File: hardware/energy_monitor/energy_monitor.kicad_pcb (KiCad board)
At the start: 2 copper layers, 102.8 x 86.9 mm, 137 parts, among them J1 Screw_Terminal_01x03, J2 SJ1-3533NG, J3 SJ1-3533NG, J4 SJ1-3533NG, J5 SJ1-3533NG, J6 SJ1-3533NG, J7 SJ1-3533NG, J8 USB_OTG, Q1 MMBT2222, Q2 MMBT2222, U1 RAC04, U2 TPS730, U3 TPS723, U4 ADS131E08, U5 AP2112, U6 ESP-WROOM-32U, U7 CP2104

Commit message: Working on layout
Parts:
- F1, F2: footprint Fuse_Holders_and_Fuses:Fuseholder5x20_horiz_open_inline_Type-I -> footprint:Fuse_Littelfuse-443
- RV1, RV2: footprint Varistors:RV_Disc_D15.5_W6.8_P7.5 -> Varistors:RV_Disc_D12_W5_P7.5
- moved U7 114.8 mm to (159.0, 53.1)
- moved RV1 93.6 mm to (100.7, 90.7), turned to 270 degrees
- moved F2 84.8 mm to (111.0, 94.5), turned to 270 degrees
- moved F1 79.5 mm to (93.8, 94.5), turned to 270 degrees
- moved C15 65.2 mm to (31.3, 110.9)
- moved U3 63.7 mm to (48.0, 121.7)
- moved U5 55.2 mm to (60.2, 114.9)
- moved RV2 54.3 mm to (104.3, 98.2), turned to 90 degrees
- moved U2 48.3 mm to (35.3, 127.4)
- moved C16 47.9 mm to (45.1, 108.9)
- moved U6 26.4 mm to (178.3, 57.0)
- moved J8 22.7 mm to (158.7, 33.0)
- moved J2 13.8 mm to (120.0, 119.0)
- moved U4 13.5 mm to (146.4, 76.3)
- moved J4 13.1 mm to (152.8, 119.0)
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
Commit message: Configured design rules
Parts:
- moved Q1 35.5 mm to (30.1, 139.3)
- moved Q2 35.5 mm to (40.4, 136.9)
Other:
- copper layers 2 -> 4
- net class Default: clearance 0.2 -> 0.1524; trace_width 0.25 -> 0.1524; via_dia 0.6 -> 0.452; via_drill 0.4 -> 0.3
- rule trace_clearance: 0.2 -> 0.1524
- rule trace_min: 0.2 -> 0.1524
- rule via_min_size: 0.4 -> 0.452
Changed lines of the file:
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@@
     (links 312)
     (no_connects 312)
-    (area 89.924999 33.024999 192.875001 120.075001)
+    (area 26.374999 31.525 192.900001 188.72)
     (thickness 1.6)
     (drawings 14)
@@
   (layers
     (0 F.Cu signal)
+    (1 In1.Cu signal)
+    (2 In2.Cu signal)
     (31 B.Cu signal)
-    (32 B.Adhes user)
-    (33 F.Adhes user)
-    (34 B.Paste user)
-    (35 F.Paste user)
+    (34 B.Paste user hide)
+    (35 F.Paste user hide)
     (36 B.SilkS user)
     (37 F.SilkS user)
-    (38 B.Mask user)
-    (39 F.Mask user)
-    (40 Dwgs.User user)
-    (41 Cmts.User user)
+    (38 B.Mask user hide)
+    (39 F.Mask user hide)
+    (40 Dwgs.User user hide)
     (42 Eco1.User user)
-    (43 Eco2.User user)
     (44 Edge.Cuts user)
-    (45 Margin user)
-    (46 B.CrtYd user)
-    (47 F.CrtYd user)
-    (48 B.Fab user)
+    (48 B.Fab user hide)
     (49 F.Fab user)
   )
   (setup
-    (last_trace_width 0.25)
-    (trace_clearance 0.2)
+    (last_trace_width 0.1524)
+    (user_trace_width 0.16)
+    (user_trace_width 0.2)
+    (user_trace_width 0.3)
+    (user_trace_width 0.4)
+    (trace_clearance 0.1524)
     (zone_clearance 0.508)
     (zone_45_only no)
-    (trace_min 0.2)
+    (trace_min 0.1524)
     (segment_width 0.2)
     (edge_width 0.15)
-    (via_size 0.6)
-    (via_drill 0.4)
-    (via_min_size 0.4)
+    (via_size 0.452)
+    (via_drill 0.3)
+    (via_min_size 0.452)
     (via_min_drill 0.3)
-    (uvia_size 0.3)
-    (uvia_drill 0.1)
+    (user_via 0.452 0.3)
+    (user_via 0.552 0.4)
+    (uvia_size 0.452)
+    (uvia_drill 0.3)
     (uvias_allowed no)
-    (uvia_min_size 0.2)
-    (uvia_min_drill 0.1)
+    (uvia_min_size 0.452)
+    (uvia_min_drill 0.3)
     (pcb_text_width 0.3)
     (pcb_text_size 1.5 1.5)
@@
   (net 130 "Net-(U7-Pad24)")
   (net_class Default "This is the default net class."
-    (clearance 0.2)
-    (trace_width 0.25)
-    (via_dia 0.6)
-    (via_drill 0.4)
-    (uvia_dia 0.3)
-    (uvia_drill 0.1)
+    (clearance 0.1524)
+    (trace_width 0.1524)
+    (via_dia 0.452)
+    (via_drill 0.3)
+    (uvia_dia 0.452)
+    (uvia_drill 0.3)
     (add_net +2.5V)
     (add_net +3V3)
@@
   )
   (module TO_SOT_Packages_SMD:SOT-23 (layer F.Cu)
-    (at 56.978571 162.445)
+    (at 30.078571 139.345)
     (descr "SOT-23, Standard")
     (tags SOT-23)
@@
   )
   (module TO_SOT_Packages_SMD:SOT-23 (layer F.Cu)
-    (at 67.328571 160.045)
+    (at 40.428571 136.945)
     (descr "SOT-23, Standard")
     (tags SOT-23)

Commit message: Working on layout
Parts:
- C31, C38: value 2.2u -> 10u
- moved D14 160.7 mm to (183.7, 101.4)
- moved C29 148.8 mm to (183.7, 96.3), turned to 180 degrees
- moved R36 137.5 mm to (149.3, 57.2)
- moved D6 135.9 mm to (206.7, 159.2)
- moved D18 134.6 mm to (161.9, 93.7)
- moved D15 131.0 mm to (155.5, 93.7), turned to 180 degrees
- moved D17 127.7 mm to (165.5, 93.7), turned to 180 degrees
- moved D13 127.2 mm to (173.7, 101.4)
- moved D21 122.6 mm to (185.5, 93.7), turned to 180 degrees
- moved R5 121.5 mm to (176.3, 132.9)
- moved D9 121.2 mm to (132.7, 93.7), turned to 180 degrees
- moved C28 120.1 mm to (173.7, 96.3), turned to 180 degrees
- moved D20 118.4 mm to (171.9, 93.7)
- moved D28 116.9 mm to (154.1, 57.2)
- moved R20 116.7 mm to (163.7, 98.4), turned to 180 degrees
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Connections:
- net GND renamed GNDA
- U4 pad 1: /I6_N -> /L1_N
- U4 pad 10: /I2_P -> /I3_P
- U4 pad 11: /I1_N -> /I4_N
- U4 pad 12: /I1_P -> /I4_P
- U4 pad 13: /L2_N -> /I5_N
- U4 pad 14: /L2_P -> /I5_P
- U4 pad 15: /L1_N -> /I6_N
- U4 pad 16: /L1_P -> /I6_P
- U4 pad 2: /I6_P -> /L1_P
- U4 pad 3: /I5_N -> /L2_N
- U4 pad 4: /I5_P -> /L2_P
- U4 pad 5: /I4_N -> /I1_N
- U4 pad 6: /I4_P -> /I1_P
- U4 pad 7: /I3_N -> /I2_N
- U4 pad 8: /I3_P -> /I2_P
- U4 pad 9: /I2_N -> /I3_N

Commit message: Working on layout
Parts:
- added D25: MBR120, footprint:SOD-123FL, F.Cu at (68.9, 127.2)
- added D26: MBR120, footprint:SOD-123FL, F.Cu at (62.2, 128.9)
- moved Q1 207.0 mm to (222.0, 61.7)
- moved Q2 207.0 mm to (232.3, 59.3)
- moved R33 167.7 mm to (226.4, 65.9)
- moved C51 163.8 mm to (206.7, 62.1)
- moved C52 159.3 mm to (154.5, 21.2)
- moved D23 156.0 mm to (226.6, 85.1)
- moved D24 155.6 mm to (235.2, 89.1)
- moved R32 152.1 mm to (236.4, 85.5)
- moved C38 149.4 mm to (148.3, 50.8), turned to 90 degrees
- moved R34 136.2 mm to (231.1, 66.5)
- moved C32 130.3 mm to (142.3, 50.4), turned to 270 degrees
- moved C53 127.8 mm to (160.5, 30.9)
- moved R31 124.2 mm to (224.9, 88.9)
- moved U3 120.4 mm to (145.2, 50.7), turned to 270 degrees
- moved R35 117.2 mm to (206.0, 57.5)
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
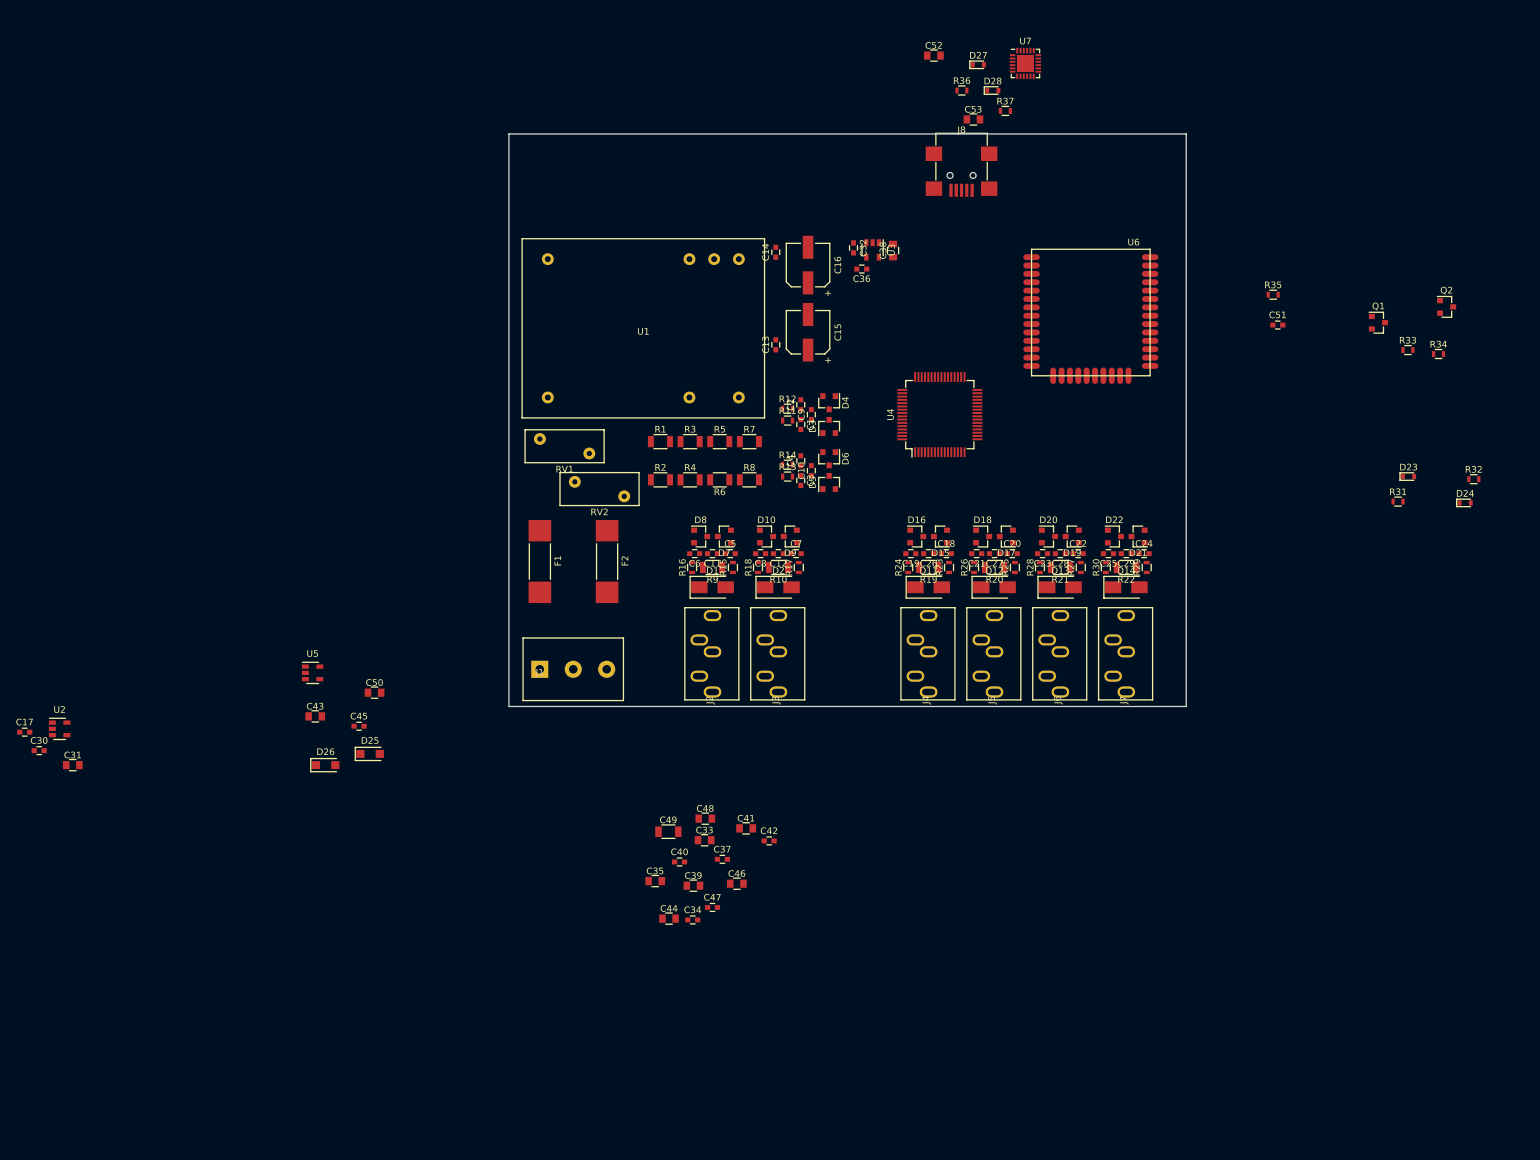
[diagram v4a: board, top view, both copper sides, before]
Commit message: Working on layout.  Removed 0.1u caps on 5V output
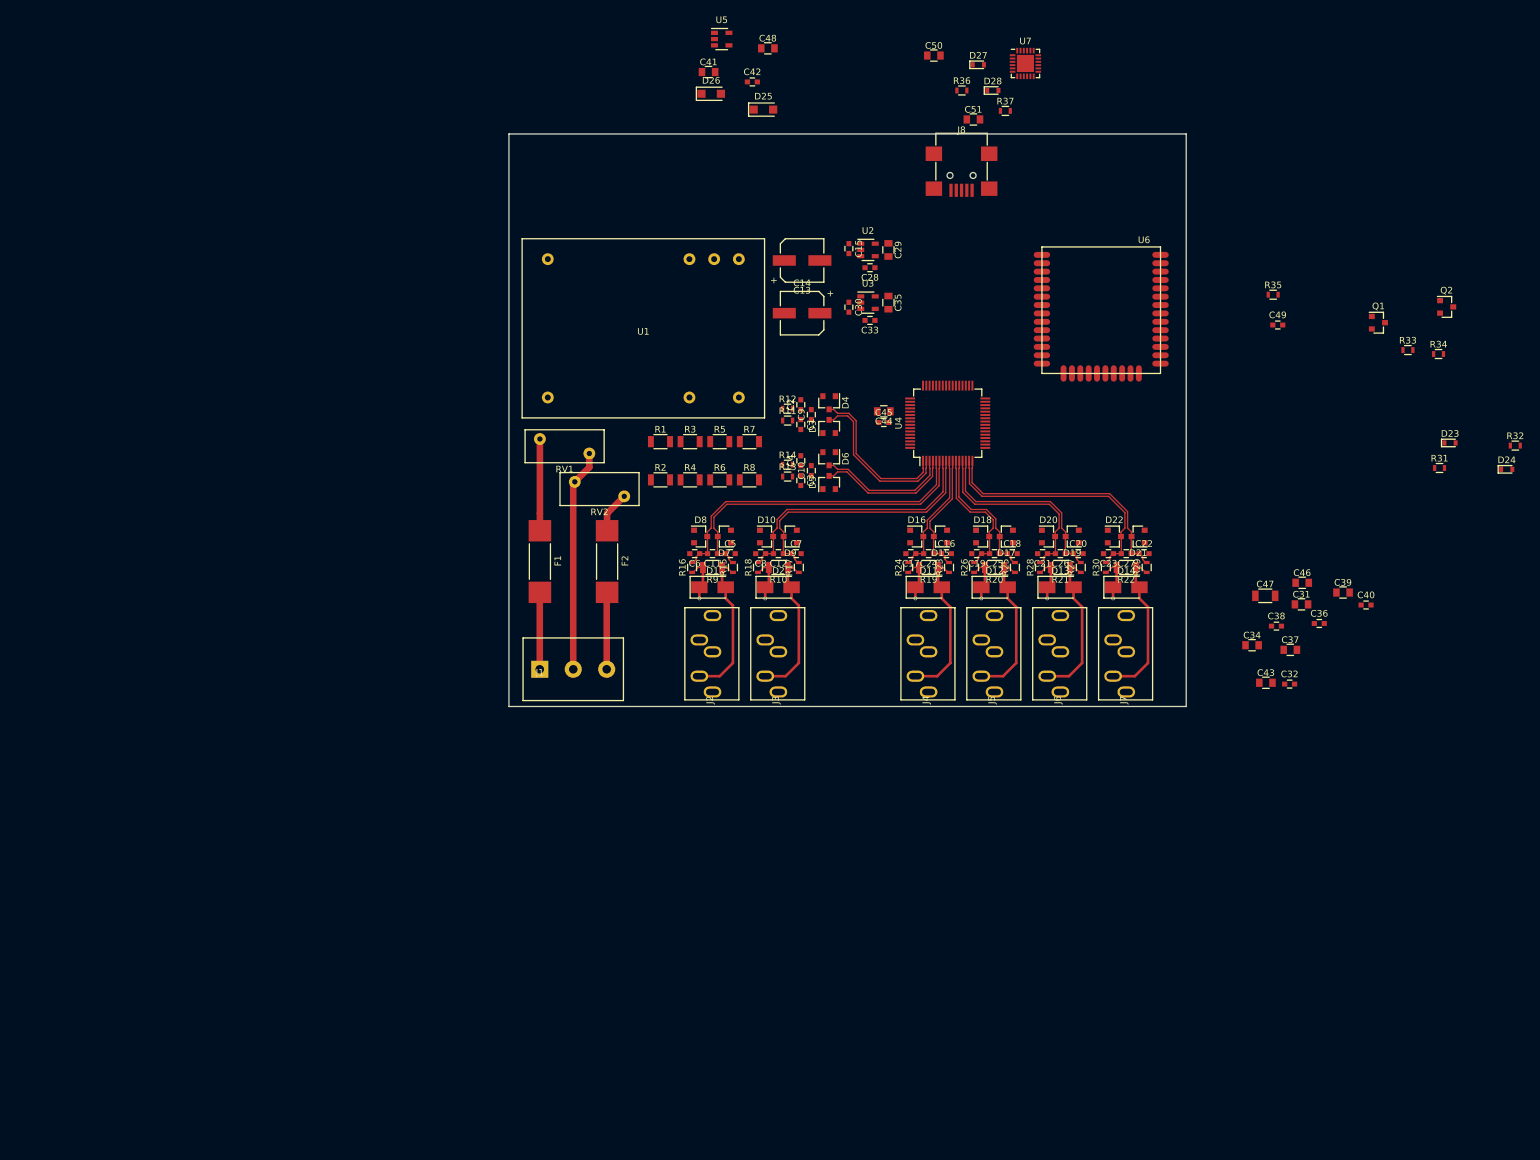
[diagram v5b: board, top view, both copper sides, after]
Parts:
- removed the C13 at (130.5, 65.1)
- removed the C14 at (130.5, 51.0)
- moved C29 146.4 mm to (147.6, 50.7), turned to 270 degrees
- moved C28 145.9 mm to (144.8, 53.4), turned to 180 degrees
- moved C15 145.0 mm to (141.6, 50.5), turned to 270 degrees
- moved U2 142.6 mm to (144.5, 50.7)
- moved D26 117.5 mm to (120.7, 27.0)
- moved C48 114.6 mm to (129.3, 20.1)
- moved D25 114.6 mm to (128.6, 29.4)
- moved C41 114.6 mm to (120.3, 23.7)
- moved C42 114.6 mm to (127.0, 25.2)
- moved U5 114.5 mm to (122.3, 18.7)
- moved C31 97.4 mm to (210.3, 104.5)
- moved C34 97.4 mm to (202.8, 110.7)
- moved C43 97.4 mm to (204.9, 116.4)
- moved C47 97.4 mm to (204.8, 103.2)
- moved C32 97.4 mm to (208.5, 116.6)
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- renumbered C15 to C13, C16 to C14, C17 to C15, C18 to C16, C19 to C17, C20 to C18, C21 to C19, C22 to C20, C23 to C21, C24 to C22, C25 to C23, C26 to C24, C27 to C25, C28 to C26, C29 to C27, C30 to C28, C31 to C29, C32 to C30, C33 to C31, C34 to C32, C36 to C33, C35 to C34, C38 to C35, C37 to C36, C39 to C37, C40 to C38, C41 to C39, C42 to C40, C43 to C41, C45 to C42, C44 to C43, C46 to C44, C47 to C45, C48 to C46, C49 to C47, C50 to C48, C51 to C49, C52 to C50, C53 to C51
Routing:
- net GNDA: track 0.00 -> 75.1 mm, vias 0 -> 6
- net /I1_N: track 0.00 -> 49.0 mm
- net /I1_P: track 0.00 -> 48.9 mm
- net /I2_N: track 0.00 -> 40.3 mm
- net /I2_P: track 0.00 -> 40.3 mm
- net /I6_P: track 0.00 -> 38.6 mm
- net /I6_N: track 0.00 -> 38.6 mm
- net /I5_P: track 0.00 -> 30.2 mm
- net /I5_N: track 0.00 -> 30.2 mm
- net /L1_P: track 0.00 -> 24.4 mm
- net /L1_N: track 0.00 -> 23.7 mm
- net Net-(D14-Pad2): track 0.00 -> 23.4 mm
- net Net-(D12-Pad2): track 0.00 -> 23.4 mm
- net Net-(D13-Pad2): track 0.00 -> 23.4 mm
- net Net-(D11-Pad2): track 0.00 -> 23.4 mm
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
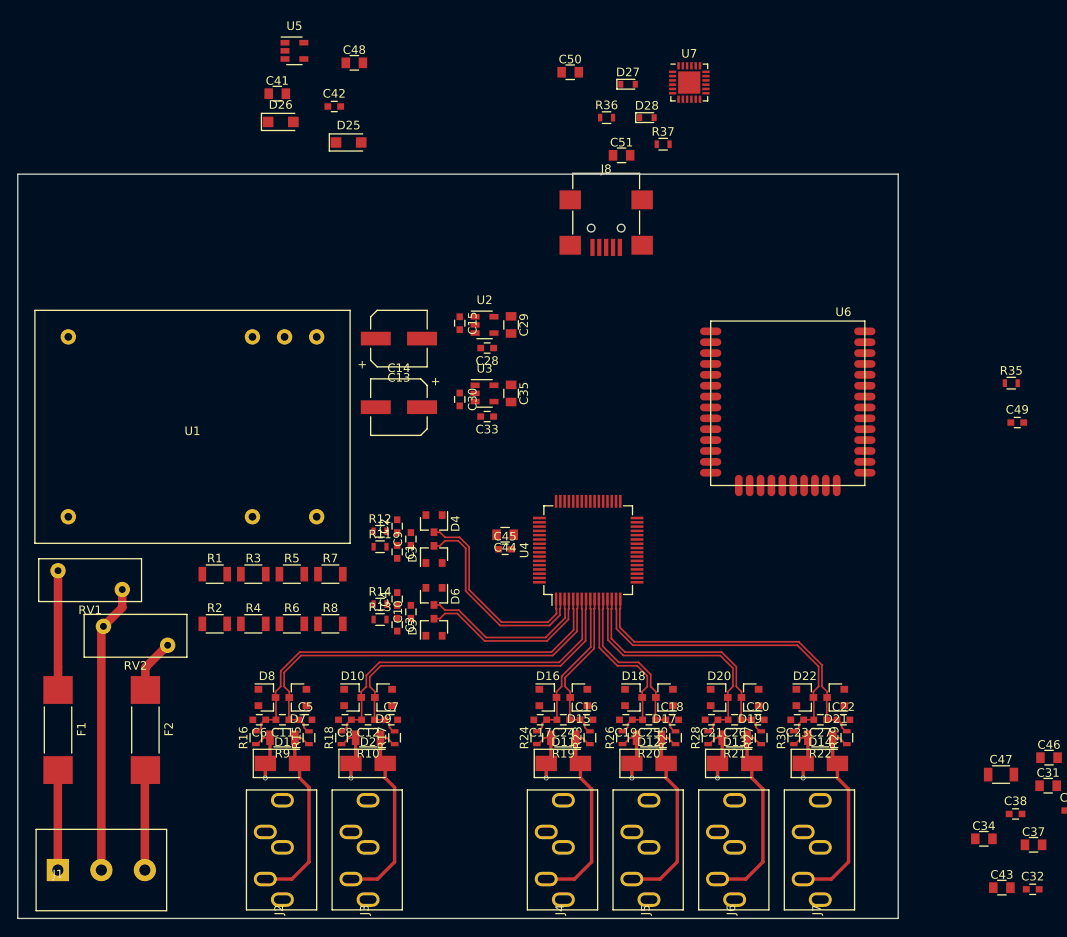
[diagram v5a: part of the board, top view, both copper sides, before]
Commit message: Switched 3.5mm jacks to terminal blocks
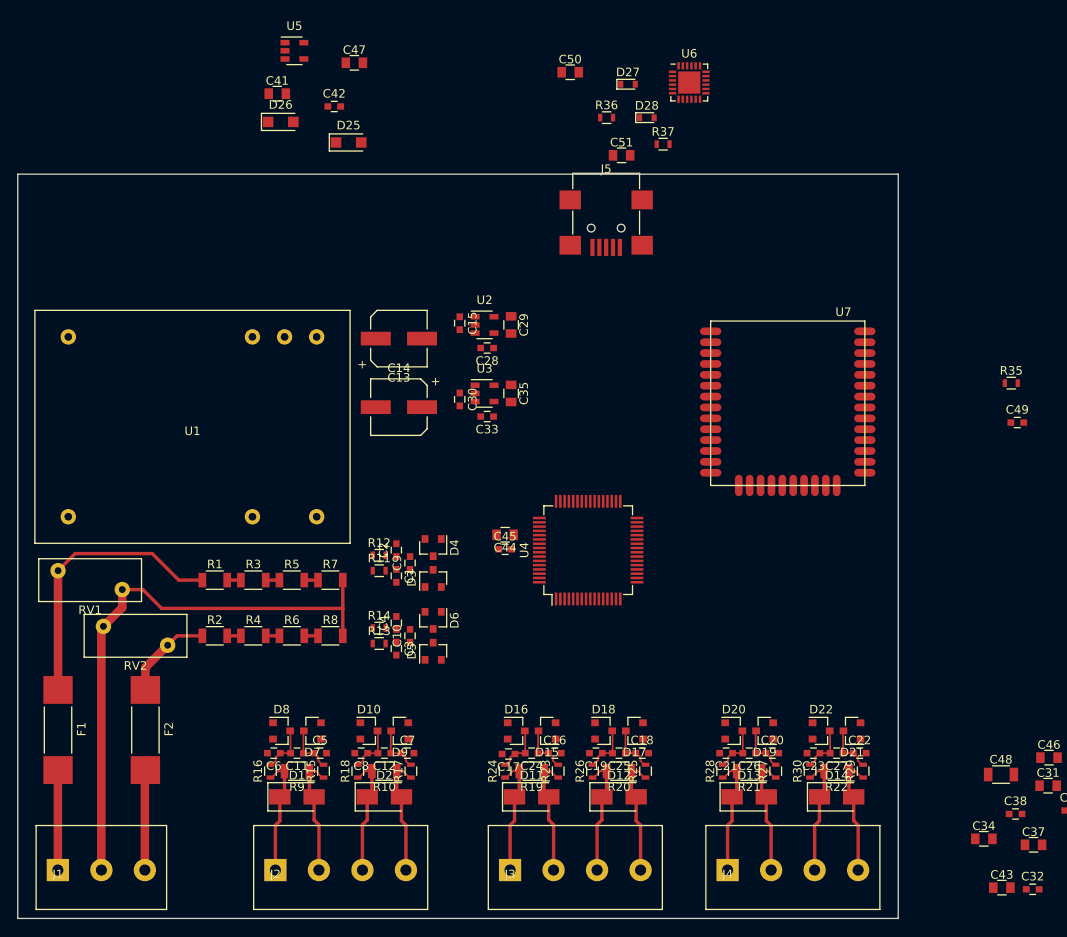
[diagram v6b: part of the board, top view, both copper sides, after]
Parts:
- removed the J5 at (162.8, 119.0)
- removed J6, J7: SJ1-3533NG, footprint:SJ1-3533NG
- J1: footprint footprint:1888690 -> footprint:TerminalBlock_03x5.08mm
- J2, J3, J4: value SJ1-3533NG -> Screw_Terminal_01x04; footprint footprint:SJ1-3533NG -> footprint:TerminalBlock_04x5.08mm
- moved J4 20.6 mm to (172.9, 114.3), turned to 0 degrees
- moved J3 18.1 mm to (147.5, 114.3), turned to 0 degrees
- moved C17 5.45 mm to (147.3, 100.8)
- moved C16 5.38 mm to (152.7, 100.7)
- moved D16 5.38 mm to (148.2, 98.1)
- moved R23 5.38 mm to (153.1, 102.8)
- moved C24 5.38 mm to (150.0, 100.7)
- moved D11 5.38 mm to (150.0, 105.8)
- moved D15 5.38 mm to (151.8, 98.1)
- moved R19 5.38 mm to (150.0, 102.8)
- moved R24 5.38 mm to (146.9, 102.8)
- moved C18 5.24 mm to (162.9, 100.7)
- moved C19 5.24 mm to (157.5, 100.7)
- moved C25 5.24 mm to (160.2, 100.7)
- moved D12 5.24 mm to (160.2, 105.8)
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- renumbered C48 to C47, C47 to C48, J8 to J5, U7 to U6, U6 to U7
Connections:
- J2 pad 3: Net-(J2-Pad3) -> GNDA
- J2 pad 4: (no net) -> Net-(D2-Pad2)
- J3 pad 2: Net-(D2-Pad2) -> Net-(D11-Pad2)
- J3 pad 3: Net-(J3-Pad3) -> GNDA
- J3 pad 4: (no net) -> Net-(D12-Pad2)
- J4 pad 2: Net-(D11-Pad2) -> Net-(D13-Pad2)
- J4 pad 3: Net-(J4-Pad3) -> GNDA
- J4 pad 4: (no net) -> Net-(D14-Pad2)
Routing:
- net GNDA: track 75.1 -> 150.7 mm, vias 6 -> 0
- net /I1_N: track 49.0 -> 5.79 mm
- net /I1_P: track 48.9 -> 5.76 mm
- net /I2_P: track 40.3 -> 5.76 mm
- net /I2_N: track 40.3 -> 5.76 mm
- net /I6_P: track 38.6 -> 5.76 mm
- net /I6_N: track 38.6 -> 5.76 mm
- net /I5_P: track 30.2 -> 5.76 mm
- net /I5_N: track 30.2 -> 5.76 mm
- net /L1_P: track 24.4 -> 0.00 mm
- net /L1_N: track 23.7 -> 0.00 mm
- net /L2_P: track 20.7 -> 0.00 mm
- net /L2_N: track 20.1 -> 0.00 mm
- net /L1: track 13.9 -> 32.9 mm
- net /I4_N: track 21.2 -> 5.76 mm
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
